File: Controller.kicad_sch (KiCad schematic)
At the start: 31 parts, among them J12 Conn_01x03_Pin, J2 Conn_01x04_Pin, J3 Conn_01x02_Pin, J4 Conn_01x02_Pin, J5 Conn_01x04_Pin, J6 Conn_01x02_Pin, U1 STM32F407VETx, U6 TL431M-0.3%-6AF, X1 X32258MOB4SI, X2 ABS07-32.768KHZ-T

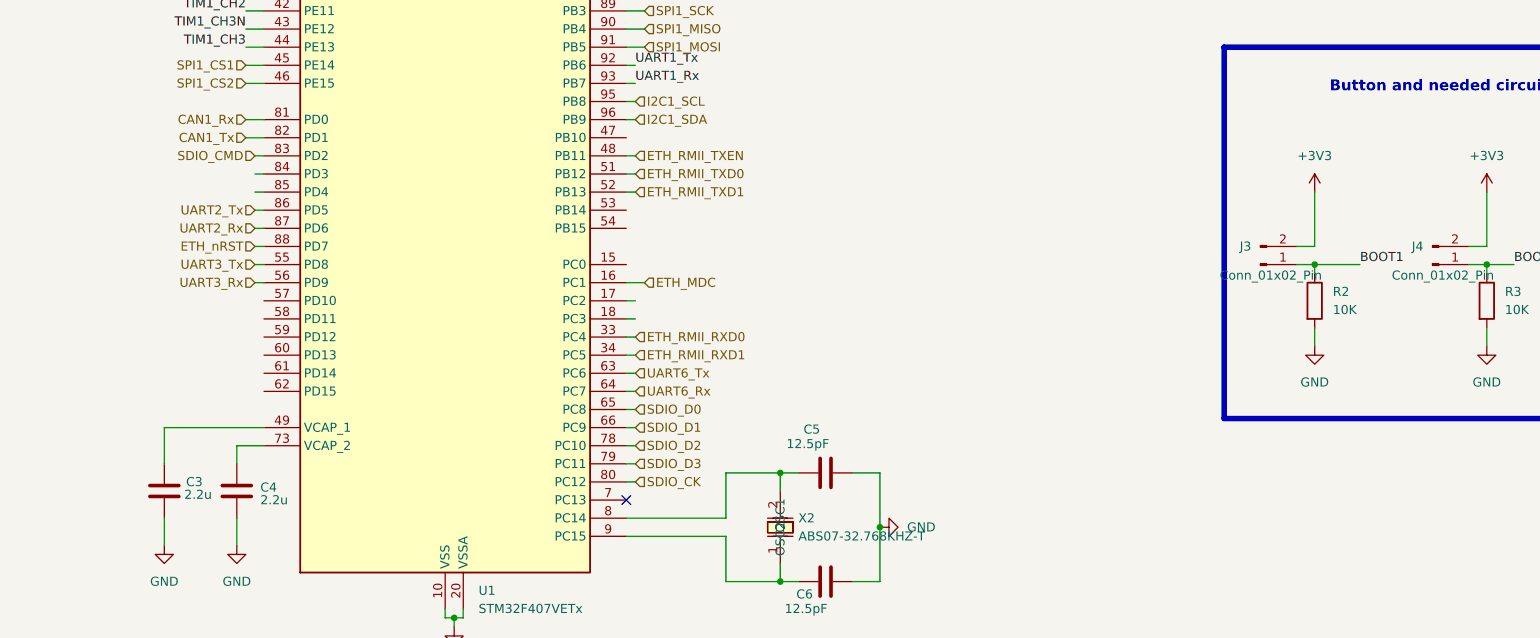
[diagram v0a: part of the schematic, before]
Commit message: Done routing for Buck Converter , Rs485 and CAN , Some Routing for MCU and associated circuitry , NO ETHERNET ROUTING , NO module Interconnects yet
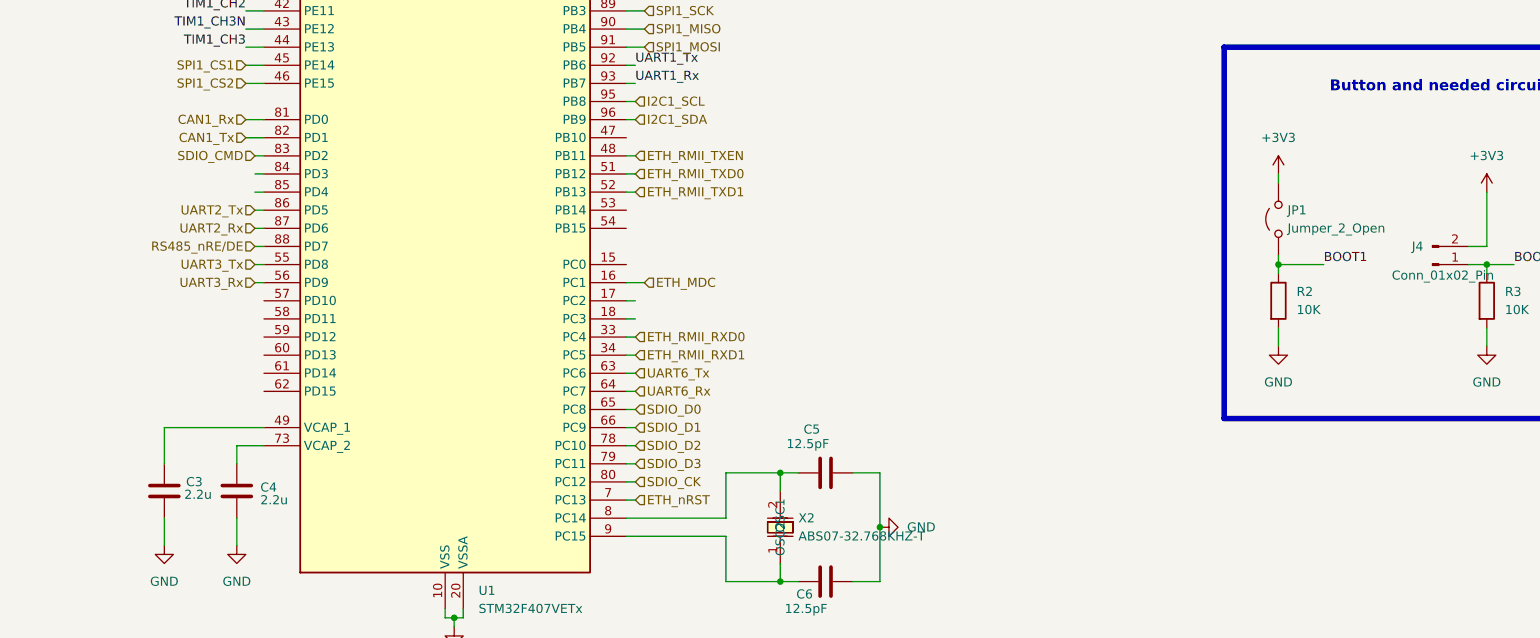
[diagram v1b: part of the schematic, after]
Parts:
- removed J3: Conn_01x02_Pin, Connector_PinHeader_2.54mm:PinHeader_1x02_P2.54mm_Vertical, symbol Connector:Conn_01x02_Pin
- added JP1: Jumper_2_Open, Jumper:SolderJumper-2_P1.3mm_Open_Pad1.0x1.5mm, symbol Jumper:Jumper_2_Open
- BT1: footprint EasyEDA:BAT_1074 -> Battery:BatteryHolder_Keystone_1060_1x2032
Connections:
- net +3V3: now also JP1.2 (B)
- net BOOT1: now also JP1.1 (A)
- net ETH_nRST: now also U1.7 (PC13); no longer U1.88 (PD7)
- new net RS485_nRE/DE: U1.88 (PD7)
- no-connect marks 1 -> 0
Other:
- moved on the sheet: R2
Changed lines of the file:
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@@
 	)
 	(junction
-		(at 207.01 134.62)
-		(diameter 0)
-		(color 0 0 0 0)
-	)
-	(junction
 		(at 85.09 34.29)
 		(diameter 0)
@@
 	)
 	(junction
+		(at 201.93 134.62)
+		(diameter 0)
+		(color 0 0 0 0)
+	)
+	(junction
 		(at 82.55 34.29)
 		(diameter 0)
@@
 		(color 0 0 0 0)
 	)
-	(no_connect
-		(at 110.49 167.64)
-	)
 	(wire
 		(pts
@@
 	(wire
 		(pts
-			(xy 204.47 132.08) (xy 207.01 132.08)
-		)
-		(stroke
-			(width 0)
-			(type default)
-		)
-	)
-	(wire
-		(pts
 			(xy 110.49 154.94) (xy 111.76 154.94)
 		)
@@
 	(wire
 		(pts
+			(xy 201.93 121.92) (xy 201.93 123.19)
+		)
+		(stroke
+			(width 0)
+			(type default)
+		)
+	)
+	(wire
+		(pts
 			(xy 77.47 27.94) (xy 77.47 38.1)
 		)
@@
 	(wire
 		(pts
-			(xy 207.01 124.46) (xy 207.01 132.08)
-		)
-		(stroke
-			(width 0)
-			(type default)
-		)
-	)
-	(wire
-		(pts
 			(xy 59.69 114.3) (xy 57.15 114.3)
 		)
@@
 	(wire
 		(pts
-			(xy 207.01 135.89) (xy 207.01 134.62)
+			(xy 201.93 135.89) (xy 201.93 134.62)
 		)
 		(stroke
@@
 	(wire
 		(pts
+			(xy 111.76 167.64) (xy 110.49 167.64)
+		)
+		(stroke
+			(width 0)
+			(type default)
+		)
+	)
+	(wire
+		(pts
 			(xy 243.84 30.48) (xy 246.38 30.48)
 		)
@@
 	(wire
 		(pts
-			(xy 207.01 143.51) (xy 207.01 146.05)
+			(xy 201.93 143.51) (xy 201.93 146.05)
 		)
 		(stroke
@@
 	(wire
 		(pts
-			(xy 204.47 134.62) (xy 207.01 134.62)
-		)
-		(stroke
-			(width 0)
-			(type default)
-		)
-	)
-	(wire
-		(pts
 			(xy 237.49 69.85) (xy 237.49 72.39)
 		)
@@
 	(wire
 		(pts
+			(xy 201.93 133.35) (xy 201.93 134.62)
+		)
+		(stroke
+			(width 0)
+			(type default)
+		)
+	)
+	(wire
+		(pts
 			(xy 80.01 34.29) (xy 82.55 34.29)
 		)
@@
 	(wire
 		(pts
+			(xy 58.42 132.08) (xy 59.69 132.08)
+		)
+		(stroke
+			(width 0)
+			(type default)
+		)
+	)
+	(wire
+		(pts
 			(xy 254 137.16) (xy 261.62 137.16)
 		)
@@
 	(wire
 		(pts
-			(xy 207.01 134.62) (xy 213.36 134.62)
+			(xy 201.93 134.62) (xy 208.28 134.62)
 		)
 		(stroke
@@
 	(wire
 		(pts
-			(xy 58.42 132.08) (xy 59.69 132.08)
-		)
-		(stroke
-			(width 0)
-			(type default)
-		)
-	)
-	(wire
-		(pts
 			(xy 50.8 54.61) (xy 50.8 63.5)
 		)
@@
 	)
 	(label "BOOT1"
-		(at 213.36 134.62 0)
+		(at 208.28 134.62 0)
 		(effects
 			(font
@@
 	(hierarchical_label "ETH_nRST"
 		(shape input)
-		(at 58.42 132.08 180)
+		(at 111.76 167.64 0)
 		(effects
 			(font
 				(size 1.27 1.27)
 			)
-			(justify right)
+			(justify left)
 		)
 	)
@@
 		)
 	)
+	(hierarchical_label "RS485_nRE{slash}DE"
+		(shape input)
+		(at 58.42 132.08 180)
+		(effects
+			(font
+				(size 1.27 1.27)
+			)
+			(justify right)
+		)
+	)
 	(hierarchical_label "SPI1_CS2"
 		(shape input)
@@
 		(on_board yes)
 		(dnp no)
-		(fields_autoplaced yes)
 		(property "Reference" "BT1"
 			(at 66.04 31.1784 0)
@@
 			)
 		)
-		(property "Footprint" "EasyEDA:BAT_1074"
-			(at 62.23 32.766 90)
+		(property "Footprint" "Battery:BatteryHolder_Keystone_1060_1x2032"
+			(at 58.42 49.53 90)
 			(effects
 				(font
@@
 	)
 	(symbol
-		(lib_id "Connector:Conn_01x02_Pin")
-		(at 199.39 134.62 0)
-		(mirror x)
-		(unit 1)
-		(exclude_from_sim no)
-		(in_bom yes)
-		(on_board yes)
-		(dnp no)
-		(property "Reference" "J3"
-			(at 198.12 132.0799 0)
-			(effects
-				(font
-					(size 1.27 1.27)
-				)
-				(justify right)
-			)
-		)
-		(property "Value" "Conn_01x02_Pin"
-			(at 208.026 136.144 0)
-			(effects
-				(font
-					(size 1.27 1.27)
-				)
-				(justify right)
-			)
-		)
-		(property "Footprint" "Connector_PinHeader_2.54mm:PinHeader_1x02_P2.54mm_Vertical"
-			(at 199.39 134.62 0)
-			(effects
-				(font
-					(size 1.27 1.27)
-				)
-				(hide yes)
-			)
-		)
-		(property "Datasheet" "~"
-			(at 199.39 134.62 0)
-			(effects
-				(font
-					(size 1.27 1.27)
-				)
-				(hide yes)
-			)
-		)
-		(property "Description" "Generic connector, single row, 01x02, script generated"
-			(at 199.39 134.62 0)
-			(effects
-				(font
-					(size 1.27 1.27)
-				)
-				(hide yes)
-			)
-		)
-		(pin "1"
-		)
-		(pin "2"
-		)
-		(instances
-			(project "OhWare"
-				(path "/38f33acd-ac87-4918-9c1f-d78977d10c9f/3373f7d9-a1d2-42db-a119-cf0259ab0da6"
-					(reference "J3")
-					(unit 1)
-				)
-			)
-		)
-	)
-	(symbol
 		(lib_id "power:GND")
 		(at 36.83 73.66 0)
@@
 	(symbol
 		(lib_id "power:+3V3")
-		(at 207.01 124.46 0)
+		(at 201.93 121.92 0)
 		(unit 1)
 		(exclude_from_sim no)
@@
 		(fields_autoplaced yes)
 		(property "Reference" "#PWR014"
-			(at 207.01 128.27 0)
+			(at 201.93 125.73 0)
 			(effects
 				(font
@@
 		)
 		(property "Value" "+3V3"
-			(at 207.01 119.38 0)
+			(at 201.93 116.84 0)
 			(effects
 				(font
@@
 		)
 		(property "Footprint" ""
-			(at 207.01 124.46 0)
+			(at 201.93 121.92 0)
 			(effects
 				(font
@@
 		)
 		(property "Datasheet" ""
-			(at 207.01 124.46 0)
+			(at 201.93 121.92 0)
 			(effects
 				(font
@@
 		)
 		(property "Description" "Power symbol creates a global label with name \"+3V3\""
-			(at 207.01 124.46 0)
+			(at 201.93 121.92 0)
 			(effects
 				(font
@@
 	(symbol
 		(lib_id "Device:R")
-		(at 207.01 139.7 0)
+		(at 201.93 139.7 0)
 		(unit 1)
 		(exclude_from_sim no)
@@
 		(fields_autoplaced yes)
 		(property "Reference" "R2"
-			(at 209.55 138.4299 0)
+			(at 204.47 138.4299 0)
 			(effects
 				(font
@@
 		)
 		(property "Value" "10K"
-			(at 209.55 140.9699 0)
+			(at 204.47 140.9699 0)
 			(effects
 				(font
@@
 		)
 		(property "Footprint" "Resistor_SMD:R_0805_2012Metric"
-			(at 205.232 139.7 90)
+			(at 200.152 139.7 90)
 			(effects
 				(font
@@
 		)
 		(property "Datasheet" "~"
-			(at 207.01 139.7 0)
+			(at 201.93 139.7 0)
 			(effects
 				(font
@@
 		)
 		(property "Description" "Resistor"
-			(at 207.01 139.7 0)
+			(at 201.93 139.7 0)
 			(effects
 				(font
@@
 	(symbol
 		(lib_id "power:GND")
-		(at 207.01 146.05 0)
+		(at 201.93 146.05 0)
 		(unit 1)
 		(exclude_from_sim no)
@@
 		(fields_autoplaced yes)
 		(property "Reference" "#PWR015"
-			(at 207.01 152.4 0)
+			(at 201.93 152.4 0)
 			(effects
 				(font
@@
 		)
 		(property "Value" "GND"
-			(at 207.01 151.13 0)
+			(at 201.93 151.13 0)
 			(effects
 				(font
@@
 		)
 		(property "Footprint" ""
-			(at 207.01 146.05 0)
+			(at 201.93 146.05 0)
 			(effects
 				(font
@@
 		)
 		(property "Datasheet" ""
-			(at 207.01 146.05 0)
+			(at 201.93 146.05 0)
 			(effects
 				(font
@@
 		)
 		(property "Description" "Power symbol creates a global label with name \"GND\" , ground"
-			(at 207.01 146.05 0)
+			(at 201.93 146.05 0)
 			(effects
 				(font
@@
 					(unit 1)
 				)
+			)
+		)
+	)
+	(symbol
+		(lib_id "Jumper:Jumper_2_Open")
+		(at 201.93 128.27 90)
+		(unit 1)
+		(exclude_from_sim no)
+		(in_bom yes)
+		(on_board yes)
+		(dnp no)
+		(fields_autoplaced yes)
+		(property "Reference" "JP1"
+			(at 203.2 126.9999 90)
+			(effects
+				(font
+					(size 1.27 1.27)
+				)
+				(justify right)
+			)
+		)
+		(property "Value" "Jumper_2_Open"
+			(at 203.2 129.5399 90)
+			(effects
+				(font
+					(size 1.27 1.27)
+				)
+				(justify right)
+			)
+		)
+		(property "Footprint" "Jumper:SolderJumper-2_P1.3mm_Open_Pad1.0x1.5mm"
+			(at 201.93 128.27 0)
+			(effects
+				(font
+					(size 1.27 1.27)
+				)
+				(hide yes)
+			)
+		)
+		(property "Datasheet" "~"
+			(at 201.93 128.27 0)
+			(effects
+				(font
+					(size 1.27 1.27)
+				)
+				(hide yes)
+			)
+		)
+		(property "Description" "Jumper, 2-pole, open"
+			(at 201.93 128.27 0)
+			(effects
+				(font
+					(size 1.27 1.27)
+				)
+				(hide yes)
+			)
+		)
+		(pin "1"
+		)
+		(pin "2"
+		)
+		(instances
+			(project ""
+				(path "/38f33acd-ac87-4918-9c1f-d78977d10c9f/3373f7d9-a1d2-42db-a119-cf0259ab0da6"
+					(reference "JP1")
+					(unit 1)
+				)

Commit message: Added Base
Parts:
- removed BT1: CR2032, Battery:BatteryHolder_Keystone_1060_1x2032, symbol Device:Battery_Cell
- removed C1, C2: 20p, Capacitor_SMD:C_0805_2012Metric, symbol Device:C
- removed C10, C11, C12, C13, C23, C7, C8, C9: 100n, Capacitor_SMD:C_0805_2012Metric, symbol Device:C
- removed C14: 4.7u, Capacitor_SMD:C_0805_2012Metric, symbol Device:C
- removed C3, C4: 2.2u, Capacitor_SMD:C_0805_2012Metric, symbol Device:C
- removed C5, C6: 12.5pF, Capacitor_SMD:C_0805_2012Metric, symbol Device:C
- removed J12: Conn_01x03_Pin, Connector_PinHeader_2.54mm:PinHeader_1x03_P2.54mm_Vertical, symbol Connector:Conn_01x03_Pin
- removed J2, J5: Conn_01x04_Pin, Connector_PinHeader_2.54mm:PinHeader_1x04_P2.54mm_Vertical, symbol Connector:Conn_01x04_Pin
- removed J4, J6: Conn_01x02_Pin, Connector_PinHeader_2.54mm:PinHeader_1x02_P2.54mm_Vertical, symbol Connector:Conn_01x02_Pin
- removed JP1: Jumper_2_Open, Jumper:SolderJumper-2_P1.3mm_Open_Pad1.0x1.5mm, symbol Jumper:Jumper_2_Open
- removed R1, R2, R3, R4: 10K, Resistor_SMD:R_0805_2012Metric, symbol Device:R
- removed R17: 1k, Resistor_SMD:R_0805_2012Metric, symbol Device:R
- removed U1: STM32F407VETx, Package_QFP:LQFP-100_14x14mm_P0.5mm, symbol MCU_ST_STM32F4:STM32F407VETx
- removed U6: TL431M-0.3%-6AF, EasyEDA:SOT-23-3_L2.9-W1.6-P1.90-LS2.8-BR, symbol EasyEDA:TL431M-0.3%-6AF
- removed X1: X32258MOB4SI, EasyEDA:CRYSTAL-SMD_4P-L3.2-W2.5-BL, symbol EasyEDA:X32258MOB4SI
- removed X2: ABS07-32.768KHZ-T, EasyEDA:OSC-SMD_2P-L3.2-W1.5, symbol EasyEDA:ABS07-32.768KHZ-T
- added U1: ~, libMain:WeAct_STM32F12, symbol libMain:WeAct_Stm32F12
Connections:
- net GND: now also U1.2 (GND), U1.26 (GND), U1.28 (GND), U1.30 (GND), U1.32 (GND), U1.59 (GND), U1.60 (GND)
- new net +3.3V: U1.1 (VB), U1.25 (3.3), U1.27 (3.3), U1.29 (3.3)
- no-connect marks 0 -> 2
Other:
- note removed: "Button and needed circuitry for RESET and BOOT"
- note removed: "HSE and LSE circuitry based on https://github.com/AlexanderDev/stm32f4discovery/blob/master/doc/schematics.pdf"

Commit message: Latest Changes
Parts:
- added D3, D6, D7: LED, LED_SMD:LED_1206_3216Metric_Pad1.42x1.75mm_HandSolder, symbol Device:LED
- added R10, R11, R7: 1k, Resistor_SMD:R_1206_3216Metric_Pad1.30x1.75mm_HandSolder, symbol Device:R
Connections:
- net +3.3V: now also R10.1, R11.1, R7.1
- net USART3_RX: now reaches U1.23 (B11)
- net USART3_TX: now reaches U1.24 (B10)
- net CAN1_TX: now reaches U1.31 (B9)
- net CAN1_RX: now reaches U1.34 (B8)
- net SPI3_DEN: now reaches U1.4 (C13)
- new net: D7.2 (A), R11.2
- new net: D6.2 (A), R10.2
- new net: D3.2 (A), R7.2
- new net INDC_LED0: D3.1 (K)
- new net INDC_LED1: D6.1 (K)
- new net INDC_LED2: D7.1 (K)
- no-connect marks 2 -> 10
